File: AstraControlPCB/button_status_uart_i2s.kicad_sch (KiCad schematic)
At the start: 16 parts, among them CN10 JST_ZH_6PIN_1A_250V, CN8 4P JST ZH, CN9 4P JST ZH

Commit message: Update wks file
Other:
- company: (none) -> LiveAstra Technologies
- title: Button, Status LED, UART, I2S -> AstraControl - Root
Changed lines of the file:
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@@
 	(paper "A4")
 	(title_block
-		(title "Button, Status LED, UART, I2S")
+		(title "AstraControl - Root")
+		(date "2024-08-26")
+		(rev "A")
+		(company "LiveAstra Technologies")
 	)
 	(junction

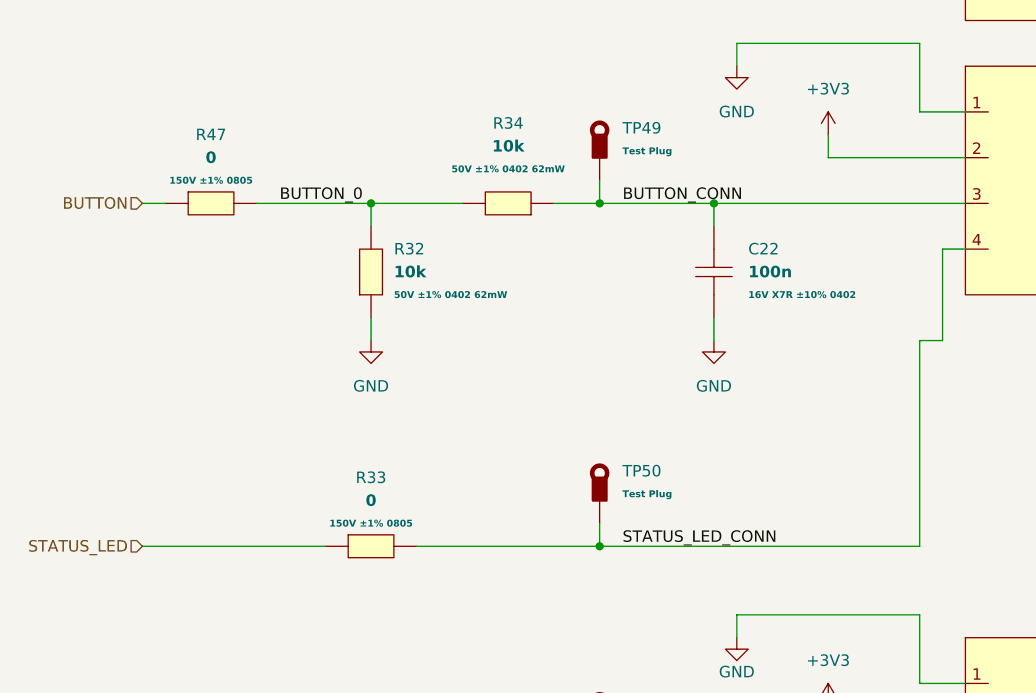
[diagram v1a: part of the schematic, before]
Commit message: Remove plus minus symbol
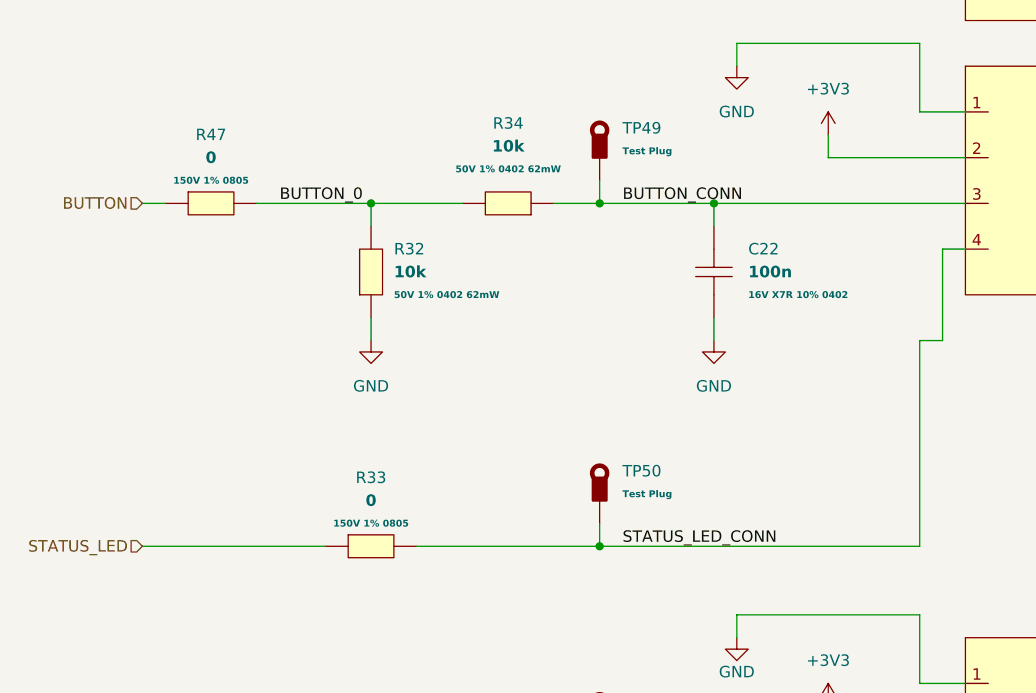
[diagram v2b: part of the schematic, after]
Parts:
- C22: Extra Values 16V X7R ±10% 0402 -> 16V X7R 10% 0402
- R32, R34: Extra Values 50V ±1% 0402 62mW -> 50V 1% 0402 62mW
- R33, R47: Extra Values 150V ±1% 0805 -> 150V 1% 0805
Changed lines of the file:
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@@
-			)
-		)
-		(property "Extra Value" ""
-			(at 127 132.08 0)
-			(effects
-				(font
-					(size 1.27 1.27)
-				)
-				(hide yes)
 			)
 		)
@@
 			)
 		)
-		(property "Extra Value" ""
-			(at 172.72 38.1 0)
-			(effects
-				(font
-					(size 1.27 1.27)
-				)
-				(hide yes)
-			)
-		)
 		(pin "1"
 		)
@@
 			)
 		)
-		(property "Extra Value" ""
-			(at 127 68.58 0)
-			(effects
-				(font
-					(size 1.27 1.27)
-				)
-				(hide yes)
-			)
-		)
 		(pin "1"
 		)
@@
 		(dnp no)
 		(fields_autoplaced yes)
-		(property "Reference" "#PWR082"
+		(property "Reference" "#PWR82"
 			(at 152.4 67.31 0)
 			(effects
@@
 			(project "AstraControl"
 				(path "/9a751838-dce8-4d69-8a02-736625ac74e7/0db21d8e-3390-4d67-877f-0e5d98e37848/457d2566-de00-4e8c-b469-a22ed41e6193"
-					(reference "#PWR082")
+					(reference "#PWR82")
 					(unit 1)
 				)
@@
 			)
 		)
-		(property "Extra Value" ""
-			(at 127 106.68 0)
-			(effects
-				(font
-					(size 1.27 1.27)
-				)
-				(hide yes)
-			)
-		)
 		(pin "1"
 		)
@@
 			)
 		)
-		(property "Extra Value" ""
-			(at 127 180.34 0)
-			(effects
-				(font
-					(size 1.27 1.27)
-				)
-				(hide yes)
-			)
-		)
 		(pin "1"
 		)
@@
 		(dnp no)
 		(fields_autoplaced yes)
-		(property "Reference" "#PWR078"
+		(property "Reference" "#PWR78"
 			(at 142.24 31.75 0)
 			(effects
@@
 			(project "AstraControl"
 				(path "/9a751838-dce8-4d69-8a02-736625ac74e7/0db21d8e-3390-4d67-877f-0e5d98e37848/457d2566-de00-4e8c-b469-a22ed41e6193"
-					(reference "#PWR078")
+					(reference "#PWR78")
 					(unit 1)
 				)
@@
 		(dnp no)
 		(fields_autoplaced yes)
-		(property "Reference" "#PWR081"
+		(property "Reference" "#PWR81"
 			(at 142.24 62.23 0)
 			(effects
@@
 			(project "AstraControl"
 				(path "/9a751838-dce8-4d69-8a02-736625ac74e7/0db21d8e-3390-4d67-877f-0e5d98e37848/457d2566-de00-4e8c-b469-a22ed41e6193"
-					(reference "#PWR081")
+					(reference "#PWR81")
 					(unit 1)
 				)
@@
 			)
 		)
-		(property "Extra Values" "16V X7R ±10% 0402"
+		(property "Extra Values" "16V X7R 10% 0402"
 			(at 143.51 81.2799 90)
 			(effects
@@
 				)
 				(justify right)
-			)
-		)
-		(property "Extra Value" ""
-			(at 139.7 78.74 0)
-			(effects
-				(font
-					(size 1.27 1.27)
-				)
-				(hide yes)
 			)
 		)
@@
 		(dnp no)
 		(fields_autoplaced yes)
-		(property "Reference" "#PWR080"
+		(property "Reference" "#PWR80"
 			(at 152.4 36.83 0)
 			(effects
@@
 			(project "AstraControl"
 				(path "/9a751838-dce8-4d69-8a02-736625ac74e7/0db21d8e-3390-4d67-877f-0e5d98e37848/457d2566-de00-4e8c-b469-a22ed41e6193"
-					(reference "#PWR080")
+					(reference "#PWR80")
 					(unit 1)
 				)
@@
 		(on_board yes)
 		(dnp no)
-		(property "Reference" "#PWR079"
+		(property "Reference" "#PWR79"
 			(at 142.24 125.73 0)
 			(effects
@@
 			(project "AstraControl"
 				(path "/9a751838-dce8-4d69-8a02-736625ac74e7/0db21d8e-3390-4d67-877f-0e5d98e37848/457d2566-de00-4e8c-b469-a22ed41e6193"
-					(reference "#PWR079")
+					(reference "#PWR79")
 					(unit 1)
 				)
@@
 			)
 		)
-		(property "Extra Values" "50V ±1% 0402 62mW"
+		(property "Extra Values" "50V 1% 0402 62mW"
 			(at 116.84 67.31 0)
 			(effects
@@
 					(bold yes)
 				)
-			)
-		)
-		(property "Extra Value" ""
-			(at 116.84 71.12 0)
-			(effects
-				(font
-					(size 1.27 1.27)
-				)
-				(hide yes)
 			)
 		)
@@
 			)
 		)
-		(property "Extra Value" ""
-			(at 172.72 68.58 0)
-			(effects
-				(font
-					(size 1.27 1.27)
-				)
-				(hide yes)
-			)
-		)
 		(pin "1"
 		)
@@
 			)
 		)
-		(property "Extra Value" ""
-			(at 127 149.86 0)
-			(effects
-				(font
-					(size 1.27 1.27)
-				)
-				(hide yes)
-			)
-		)
 		(pin "1"
 		)
@@
 			)
 		)
-		(property "Extra Values" "150V ±1% 0805"
+		(property "Extra Values" "150V 1% 0805"
 			(at 101.6 106.68 0)
 			(effects
@@
 					(bold yes)
 				)
-			)
-		)
-		(property "Extra Value" ""
-			(at 101.6 109.22 0)
-			(effects
-				(font
-					(size 1.27 1.27)
-				)
-				(hide yes)
 			)
 		)
@@
 			)
 		)
-		(property "Extra Values" "50V ±1% 0402 62mW"
+		(property "Extra Values" "50V 1% 0402 62mW"
 			(at 104.14 81.2799 90)
 			(effects
@@
 				)
 				(justify right)
-			)
-		)
-		(property "Extra Value" ""
-			(at 101.6 78.74 0)
-			(effects
-				(font
-					(size 1.27 1.27)
-				)
-				(hide yes)
 			)
 		)
@@
 			)
 		)
-		(property "Extra Value" ""
-			(at 127 38.1 0)
-			(effects
-				(font
-					(size 1.27 1.27)
-				)
-				(hide yes)
-			)
-		)
 		(pin "1"
 		)
@@
 			)
 		)
-		(property "Extra Value" ""
-			(at 127 165.1 0)
-			(effects
-				(font
-					(size 1.27 1.27)
-				)
-				(hide yes)
-			)
-		)
 		(pin "1"
 		)
@@
 		(dnp no)
 		(fields_autoplaced yes)
-		(property "Reference" "#PWR083"
+		(property "Reference" "#PWR83"
 			(at 152.4 130.81 0)
 			(effects
@@
 			(project "AstraControl"
 				(path "/9a751838-dce8-4d69-8a02-736625ac74e7/0db21d8e-3390-4d67-877f-0e5d98e37848/457d2566-de00-4e8c-b469-a22ed41e6193"
-					(reference "#PWR083")
+					(reference "#PWR83")
 					(unit 1)
 				)
@@
 		(dnp no)
 		(fields_autoplaced yes)
-		(property "Reference" "#PWR076"
+		(property "Reference" "#PWR76"
 			(at 101.6 92.71 0)
 			(effects
@@
 			(project "AstraControl"
 				(path "/9a751838-dce8-4d69-8a02-736625ac74e7/0db21d8e-3390-4d67-877f-0e5d98e37848/457d2566-de00-4e8c-b469-a22ed41e6193"
-					(reference "#PWR076")
+					(reference "#PWR76")
 					(unit 1)
 				)
@@
 		(dnp no)
 		(fields_autoplaced yes)
-		(property "Reference" "#PWR077"
+		(property "Reference" "#PWR77"
 			(at 139.7 92.71 0)
 			(effects
@@
 			(project "AstraControl"
 				(path "/9a751838-dce8-4d69-8a02-736625ac74e7/0db21d8e-3390-4d67-877f-0e5d98e37848/457d2566-de00-4e8c-b469-a22ed41e6193"
-					(reference "#PWR077")
+					(reference "#PWR77")
 					(unit 1)
 				)
@@
 			)
 		)
-		(property "Extra Value" ""
-			(at 172.72 137.16 0)
-			(effects
-				(font
-					(size 1.27 1.27)
-				)
-				(hide yes)
-			)
-		)
 		(pin "5"
 		)
@@
 			)
 		)
-		(property "Extra Values" "150V ±1% 0805"
+		(property "Extra Values" "150V 1% 0805"
 			(at 83.82 68.58 0)
 			(effects
@@
 					(bold yes)
 				)
-			)
-		)
-		(property "Extra Value" ""
-			(at 83.82 71.12 0)
-			(effects
-				(font
-					(size 1.27 1.27)
-				)
-				(hide yes)
 			)
 		)
@@
 			)
 		)
-		(property "Extra Value" ""
-			(at 88.9 43.18 0)
-			(effects
-				(font
-					(size 1.27 1.27)
-				)
-				(hide yes)
-			)
-		)

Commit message: workflow
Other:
- note added: "HMI UART I2S"
- moved on the sheet: C22, CN10, CN8, CN9, R32, R33, R34, R47, TP48, TP49, TP50, TP51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

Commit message: update
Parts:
- renumbered C22 to C23, R47 to R40, R32 to R41, R33 to R42, R34 to R43, TP48 to TP44, TP55 to TP45, TP49 to TP46, TP50 to TP47, TP51 to TP48, TP52 to TP49, TP53 to TP50, TP54 to TP51
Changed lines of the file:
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@@
 		(dnp no)
 		(fields_autoplaced yes)
-		(property "Reference" "TP51"
+		(property "Reference" "TP48"
 			(at 139.7 123.7276 0)
 			(effects
@@
 			(project "AstraControl"
 				(path "/9a751838-dce8-4d69-8a02-736625ac74e7/0db21d8e-3390-4d67-877f-0e5d98e37848/457d2566-de00-4e8c-b469-a22ed41e6193"
-					(reference "TP51")
+					(reference "TP48")
 					(unit 1)
 				)
@@
 		(dnp no)
 		(fields_autoplaced yes)
-		(property "Reference" "TP49"
+		(property "Reference" "TP46"
 			(at 139.7 60.2276 0)
 			(effects
@@
 			(project "AstraControl"
 				(path "/9a751838-dce8-4d69-8a02-736625ac74e7/0db21d8e-3390-4d67-877f-0e5d98e37848/457d2566-de00-4e8c-b469-a22ed41e6193"
-					(reference "TP49")
+					(reference "TP46")
 					(unit 1)
 				)
@@
 		(dnp no)
 		(fields_autoplaced yes)
-		(property "Reference" "#PWR082"
+		(property "Reference" "#PWR087"
 			(at 162.56 64.77 0)
 			(effects
@@
 			(project "AstraControl"
 				(path "/9a751838-dce8-4d69-8a02-736625ac74e7/0db21d8e-3390-4d67-877f-0e5d98e37848/457d2566-de00-4e8c-b469-a22ed41e6193"
-					(reference "#PWR082")
+					(reference "#PWR087")
 					(unit 1)
 				)
@@
 		(dnp no)
 		(fields_autoplaced yes)
-		(property "Reference" "TP50"
+		(property "Reference" "TP47"
 			(at 139.7 98.3276 0)
 			(effects
@@
 			(project "AstraControl"
 				(path "/9a751838-dce8-4d69-8a02-736625ac74e7/0db21d8e-3390-4d67-877f-0e5d98e37848/457d2566-de00-4e8c-b469-a22ed41e6193"
-					(reference "TP50")
+					(reference "TP47")
 					(unit 1)
 				)
@@
 		(dnp no)
 		(fields_autoplaced yes)
-		(property "Reference" "TP54"
+		(property "Reference" "TP51"
 			(at 139.7 171.9876 0)
 			(effects
@@
 			(project "AstraControl"
 				(path "/9a751838-dce8-4d69-8a02-736625ac74e7/0db21d8e-3390-4d67-877f-0e5d98e37848/457d2566-de00-4e8c-b469-a22ed41e6193"
-					(reference "TP54")
+					(reference "TP51")
 					(unit 1)
 				)
@@
 		(dnp no)
 		(fields_autoplaced yes)
-		(property "Reference" "#PWR078"
+		(property "Reference" "#PWR083"
 			(at 152.4 29.21 0)
 			(effects
@@
 			(project "AstraControl"
 				(path "/9a751838-dce8-4d69-8a02-736625ac74e7/0db21d8e-3390-4d67-877f-0e5d98e37848/457d2566-de00-4e8c-b469-a22ed41e6193"
-					(reference "#PWR078")
+					(reference "#PWR083")
 					(unit 1)
 				)
@@
 		(dnp no)
 		(fields_autoplaced yes)
-		(property "Reference" "#PWR081"
+		(property "Reference" "#PWR084"
 			(at 152.4 59.69 0)
 			(effects
@@
 			(project "AstraControl"
 				(path "/9a751838-dce8-4d69-8a02-736625ac74e7/0db21d8e-3390-4d67-877f-0e5d98e37848/457d2566-de00-4e8c-b469-a22ed41e6193"
-					(reference "#PWR081")
+					(reference "#PWR084")
 					(unit 1)
 				)
@@
 		(dnp no)
 		(fields_autoplaced yes)
-		(property "Reference" "C22"
+		(property "Reference" "C23"
 			(at 153.67 73.6599 90)
 			(effects
@@
 			(project "AstraControl"
 				(path "/9a751838-dce8-4d69-8a02-736625ac74e7/0db21d8e-3390-4d67-877f-0e5d98e37848/457d2566-de00-4e8c-b469-a22ed41e6193"
-					(reference "C22")
+					(reference "C23")
 					(unit 1)
 				)
@@
 		(dnp no)
 		(fields_autoplaced yes)
-		(property "Reference" "#PWR080"
+		(property "Reference" "#PWR086"
 			(at 162.56 34.29 0)
 			(effects
@@
 			(project "AstraControl"
 				(path "/9a751838-dce8-4d69-8a02-736625ac74e7/0db21d8e-3390-4d67-877f-0e5d98e37848/457d2566-de00-4e8c-b469-a22ed41e6193"
-					(reference "#PWR080")
+					(reference "#PWR086")
 					(unit 1)
 				)
@@
 		(on_board yes)
 		(dnp no)
-		(property "Reference" "#PWR079"
+		(property "Reference" "#PWR085"
 			(at 152.4 123.19 0)
 			(effects
@@
 			(project "AstraControl"
 				(path "/9a751838-dce8-4d69-8a02-736625ac74e7/0db21d8e-3390-4d67-877f-0e5d98e37848/457d2566-de00-4e8c-b469-a22ed41e6193"
-					(reference "#PWR079")
+					(reference "#PWR085")
 					(unit 1)
 				)
@@
 		(dnp no)
 		(fields_autoplaced yes)
-		(property "Reference" "R34"
+		(property "Reference" "R43"
 			(at 127 59.69 0)
 			(effects
@@
 			(project "AstraControl"
 				(path "/9a751838-dce8-4d69-8a02-736625ac74e7/0db21d8e-3390-4d67-877f-0e5d98e37848/457d2566-de00-4e8c-b469-a22ed41e6193"
-					(reference "R34")
+					(reference "R43")
 					(unit 1)
 				)
@@
 		(dnp no)
 		(fields_autoplaced yes)
-		(property "Reference" "TP52"
+		(property "Reference" "TP49"
 			(at 139.7 141.5076 0)
 			(effects
@@
 			(project "AstraControl"
 				(path "/9a751838-dce8-4d69-8a02-736625ac74e7/0db21d8e-3390-4d67-877f-0e5d98e37848/457d2566-de00-4e8c-b469-a22ed41e6193"
-					(reference "TP52")
+					(reference "TP49")
 					(unit 1)
 				)
@@
 		(on_board yes)
 		(dnp no)
-		(property "Reference" "R33"
+		(property "Reference" "R42"
 			(at 111.76 99.06 0)
 			(effects
@@
 			(project "AstraControl"
 				(path "/9a751838-dce8-4d69-8a02-736625ac74e7/0db21d8e-3390-4d67-877f-0e5d98e37848/457d2566-de00-4e8c-b469-a22ed41e6193"
-					(reference "R33")
+					(reference "R42")
 					(unit 1)
 				)
@@
 		(dnp no)
 		(fields_autoplaced yes)
-		(property "Reference" "R32"
+		(property "Reference" "R41"
 			(at 114.3 73.6599 90)
 			(effects
@@
 			(project "AstraControl"
 				(path "/9a751838-dce8-4d69-8a02-736625ac74e7/0db21d8e-3390-4d67-877f-0e5d98e37848/457d2566-de00-4e8c-b469-a22ed41e6193"
-					(reference "R32")
+					(reference "R41")
 					(unit 1)
 				)
@@
 		(dnp no)
 		(fields_autoplaced yes)
-		(property "Reference" "TP55"
+		(property "Reference" "TP45"
 			(at 139.7 29.7476 0)
 			(effects
@@
 			(project "AstraControl"
 				(path "/9a751838-dce8-4d69-8a02-736625ac74e7/0db21d8e-3390-4d67-877f-0e5d98e37848/457d2566-de00-4e8c-b469-a22ed41e6193"
-					(reference "TP55")
+					(reference "TP45")
 					(unit 1)
 				)
@@
 		(dnp no)
 		(fields_autoplaced yes)
-		(property "Reference" "TP53"
+		(property "Reference" "TP50"
 			(at 139.7 156.7476 0)
 			(effects
@@
 			(project "AstraControl"
 				(path "/9a751838-dce8-4d69-8a02-736625ac74e7/0db21d8e-3390-4d67-877f-0e5d98e37848/457d2566-de00-4e8c-b469-a22ed41e6193"
-					(reference "TP53")
+					(reference "TP50")
 					(unit 1)
 				)
@@
 		(dnp no)
 		(fields_autoplaced yes)
-		(property "Reference" "#PWR083"
+		(property "Reference" "#PWR088"
 			(at 162.56 128.27 0)
 			(effects
@@
 			(project "AstraControl"
 				(path "/9a751838-dce8-4d69-8a02-736625ac74e7/0db21d8e-3390-4d67-877f-0e5d98e37848/457d2566-de00-4e8c-b469-a22ed41e6193"
-					(reference "#PWR083")
+					(reference "#PWR088")
 					(unit 1)
 				)
@@
 		(dnp no)
 		(fields_autoplaced yes)
-		(property "Reference" "#PWR076"
+		(property "Reference" "#PWR081"
 			(at 111.76 90.17 0)
 			(effects
@@
 			(project "AstraControl"
 				(path "/9a751838-dce8-4d69-8a02-736625ac74e7/0db21d8e-3390-4d67-877f-0e5d98e37848/457d2566-de00-4e8c-b469-a22ed41e6193"
-					(reference "#PWR076")
+					(reference "#PWR081")
 					(unit 1)
 				)
@@
 		(dnp no)
 		(fields_autoplaced yes)
-		(property "Reference" "#PWR077"
+		(property "Reference" "#PWR082"
 			(at 149.86 90.17 0)
 			(effects
@@
 			(project "AstraControl"
 				(path "/9a751838-dce8-4d69-8a02-736625ac74e7/0db21d8e-3390-4d67-877f-0e5d98e37848/457d2566-de00-4e8c-b469-a22ed41e6193"
-					(reference "#PWR077")
+					(reference "#PWR082")
 					(unit 1)
 				)
@@
 		(on_board yes)
 		(dnp no)
-		(property "Reference" "R47"
+		(property "Reference" "R40"
 			(at 93.98 60.96 0)
 			(effects
@@
 			(project "AstraControl"
 				(path "/9a751838-dce8-4d69-8a02-736625ac74e7/0db21d8e-3390-4d67-877f-0e5d98e37848/457d2566-de00-4e8c-b469-a22ed41e6193"
-					(reference "R47")
+					(reference "R40")
 					(unit 1)
 				)
@@
 		(dnp no)
 		(fields_autoplaced yes)
-		(property "Reference" "TP48"
+		(property "Reference" "TP44"
 			(at 101.6 34.8276 0)
 			(effects
@@
 			(project "AstraControl"
 				(path "/9a751838-dce8-4d69-8a02-736625ac74e7/0db21d8e-3390-4d67-877f-0e5d98e37848/457d2566-de00-4e8c-b469-a22ed41e6193"
-					(reference "TP48")
-					(unit 1)
-				)
+					(reference "TP44")
+					(unit 1)
+				)

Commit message: More routing
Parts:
- added INF8: ~, symbol LiveAstra:Information_Box
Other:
- note added: "ESP32-S3 WROOM has a 499Omh resistor on the TX line."
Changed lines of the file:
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@@
+		)
+	)
+	(text "ESP32-S3 WROOM has a 499Omh resistor on the TX \nline."
+		(exclude_from_sim no)
+		(at 25.4 45.72 0)
+		(effects
+			(font
+				(face "ING Me")
+				(size 1.397 1.397)
+			)
+			(justify left)
 		)
 	)
@@
 					(unit 1)
 				)
+			)
+		)
+	)
+	(symbol
+		(lib_id "LiveAstra:Information_Box")
+		(at 48.26 43.18 0)
+		(unit 1)
+		(exclude_from_sim yes)
+		(in_bom no)
+		(on_board no)
+		(dnp no)
+		(fields_autoplaced yes)
+		(property "Reference" "INF8"
+			(at 48.26 31.75 0)
+			(effects
+				(font
+					(size 1.27 1.27)
+				)
+			)
+		)
+		(property "Value" "~"
+			(at 48.26 34.29 0)
+			(effects
+				(font
+					(size 1.27 1.27)
+				)
+			)
+		)
+		(property "Footprint" ""
+			(at 33.02 39.37 0)
+			(effects
+				(font
+					(size 1.27 1.27)
+				)
+				(hide yes)
+			)
+		)
+		(property "Datasheet" ""
+			(at 33.02 39.37 0)
+			(effects
+				(font
+					(size 1.27 1.27)
+				)
+				(hide yes)
+			)
+		)
+		(property "Description" ""
+			(at 33.02 39.37 0)
+			(effects
+				(font
+					(size 1.27 1.27)
+				)
+				(hide yes)
+			)
+		)
+		(instances
+			(project ""
+				(path "/9a751838-dce8-4d69-8a02-736625ac74e7/0db21d8e-3390-4d67-877f-0e5d98e37848/457d2566-de00-4e8c-b469-a22ed41e6193"
+					(reference "INF8")
+					(unit 1)
+				)
